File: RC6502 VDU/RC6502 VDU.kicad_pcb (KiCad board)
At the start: 2 copper layers, 99.1 x 99.7 mm, 35 parts, among them J1 RC6502_Backplane, J2 VDU_BASE, J3 VIDEO, J4 Hole, J5 Hole, J6 Hole, J7 Hole, J8 RCA_PLUG, U1 MC6847, U10 74LS02, U11 VDU_Port, U12 74LS374, U2 HM62256BLP-7, U3 74LS244, U4 74LS244, U5 74LS245, U6 74LS374, U7 74HCT138, U8 74LS32, U9 74HCT138, X1 3.579545 MHz

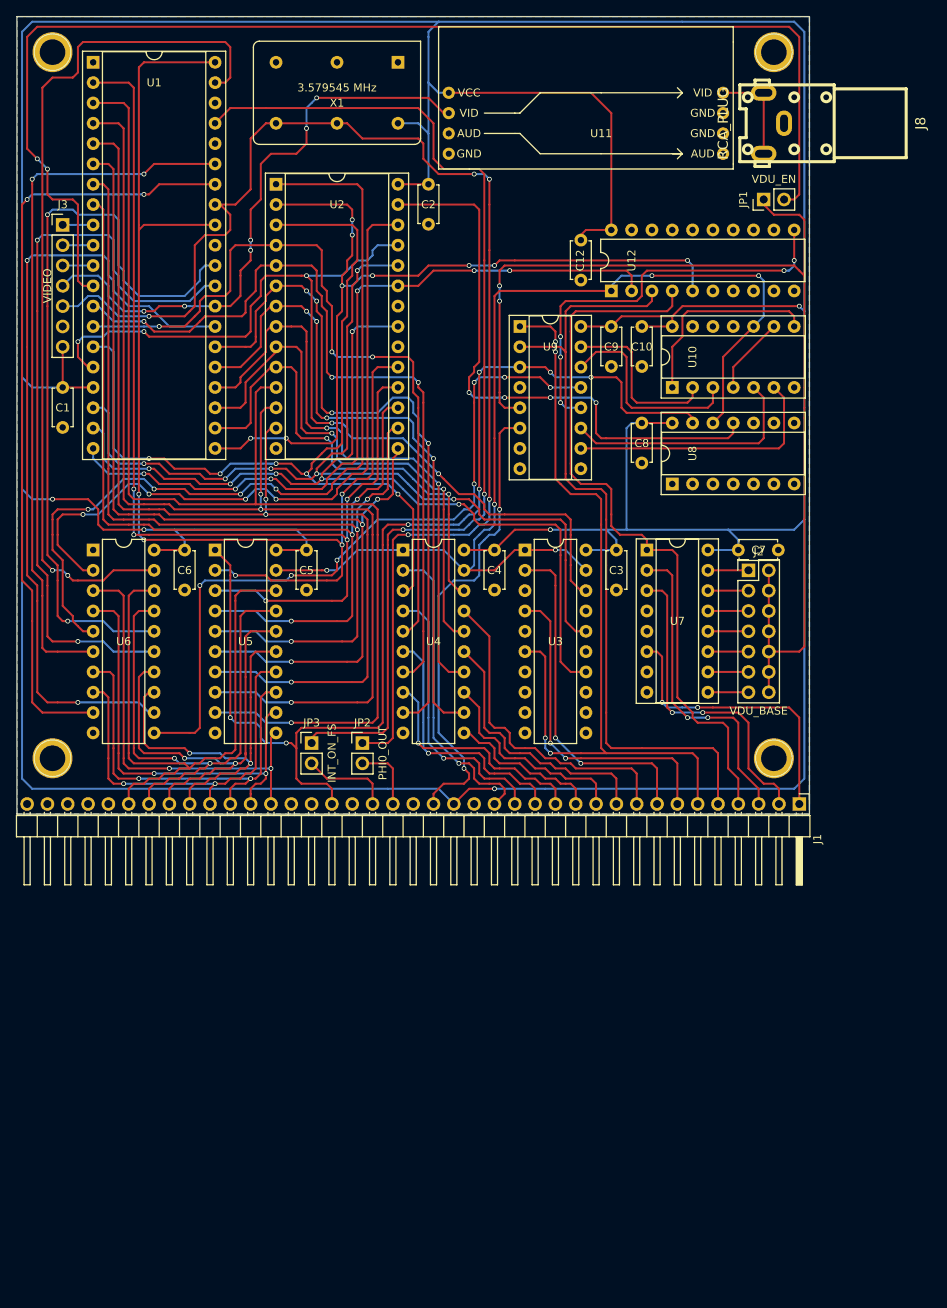
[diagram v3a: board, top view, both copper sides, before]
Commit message: Cleaned up silkscreen
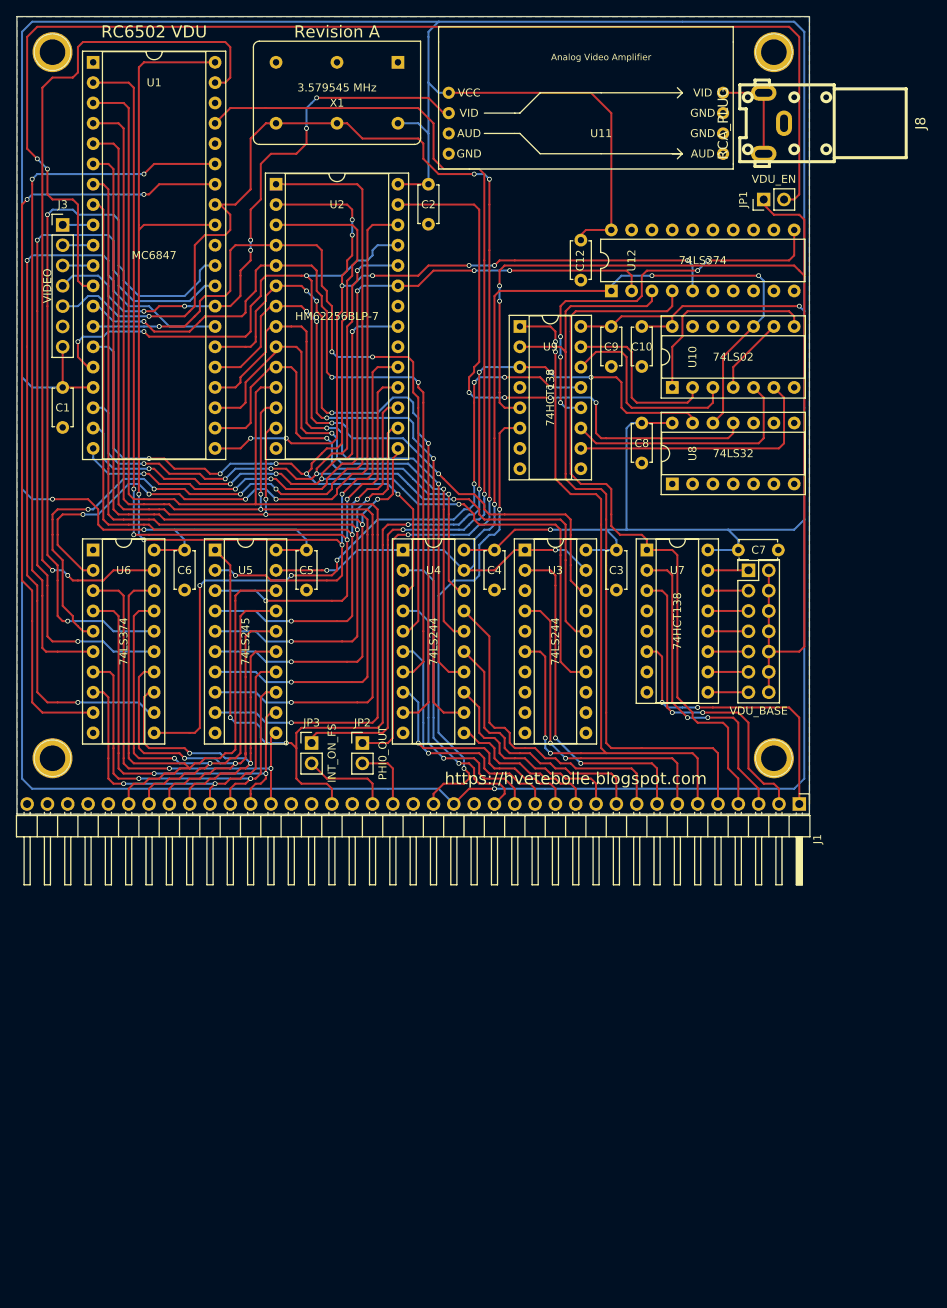
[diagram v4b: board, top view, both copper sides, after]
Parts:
- U3, U4, U5, U6: footprint Housings_DIP:DIP-20_W7.62mm -> Housings_DIP:DIP-20_W7.62mm_Socket
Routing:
- net ~REG1: track 52.1 -> 51.4 mm
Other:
- board text added: "Address Buffer #0 A00-A07"
- board text added: "Address Buffer #1 A08-A10"
- board text added: "Analog Video Amplifier"
- board text added: "Analog Video Amplifier Attach adjusted analog composite video circuit suitable for display used, added as option to test assorted design viability."
- board text added: "Data Transceiver"
- board text added: "MC6847 Video Display Generator"
- board text added: "RC6502 VDU"
- board text added: "RC6502 VDU Board Revision A https://hvetebolle.blogspot.com"
- board text added: "Register 0: [b0,1] Page select [b2] G/~A [b03] S/~A [b04] GM2 [b05] GM1 [b06] GM0 [b07] CSS"
- board text added: "Register 1: [b0,1] Video RAM Window Select (external access)"
- board text added: "Revision A"
- board text added: "VDU BASE"
- board text added: "VDU Clock NTSC freq. oscillator"
- board text added: "VDU Register 0 (Page Select/Settings) VDU_BASE + $800"
- board text added: "VDU Register 1 (Memory Window Select) VDU_BASE + $C00"
- board text added: "Video RAM VDU_BASE + [$000-$7FF] Register 0[b0-b1] 8K Page Select Register 1[b0-b1] 2K Window Select"
- board text added: "https://hvetebolle.blogspot.com"

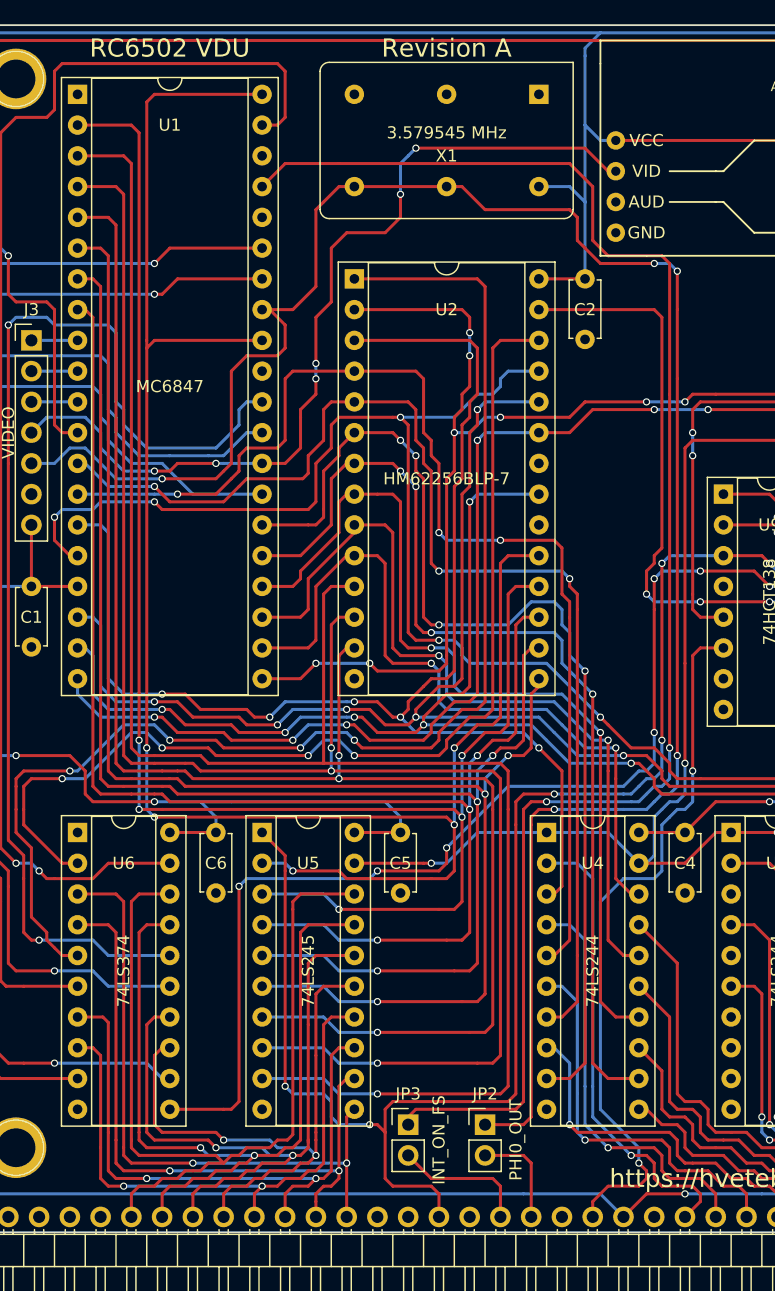
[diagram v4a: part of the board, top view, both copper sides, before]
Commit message: Tried to increase ground plane flow
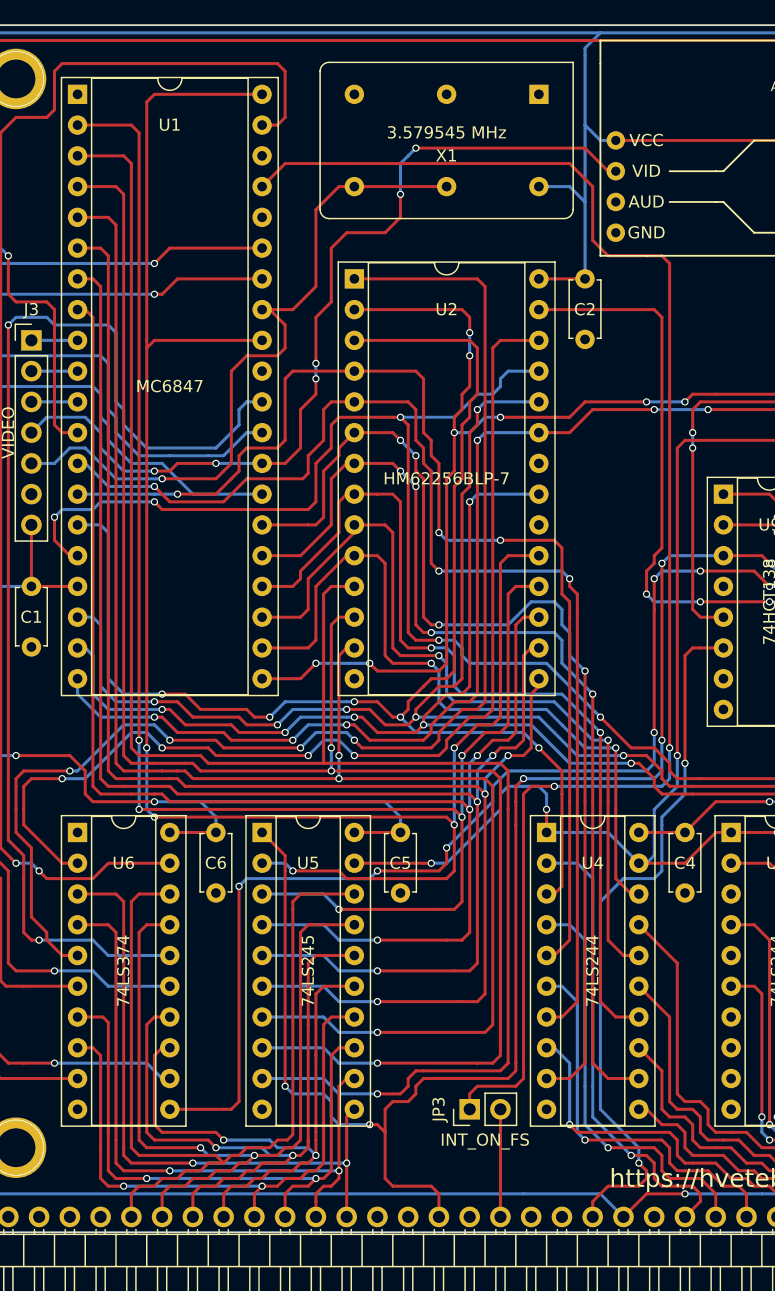
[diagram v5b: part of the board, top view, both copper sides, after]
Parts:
- removed JP2: PHI0_OUT, Pin_Headers:Pin_Header_Straight_1x02_Pitch2.54mm
- moved JP3 5.24 mm to (94.6, 134.0), turned to 90 degrees
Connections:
- J1 pad 21: PHI0 -> (no net)
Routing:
- net VDU_CLK: track 167.2 -> 59.6 mm, vias 5 -> 1
- net PHI0: track 8.52 -> 0.00 mm
- net ~CS_RAM_EXT: track 135.9 -> 141.7 mm, vias 5 -> 6
- net ~FS: track 130.9 -> 125.3 mm
- net Net-(J1-Pad22): track 11.2 -> 8.89 mm
- net VD0: track 148.8 -> 148.0 mm
- net ~REG0: track 92.4 -> 93.1 mm
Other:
- board text removed: "RC6502 VDU"
- board text removed: "Revision A"
